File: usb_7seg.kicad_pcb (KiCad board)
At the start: 2 copper layers, 72 x 47.5 mm, 8 parts, among them U1 SeeeduinoXIAO, U2 7segment_led, U3  TM1637 TM1637

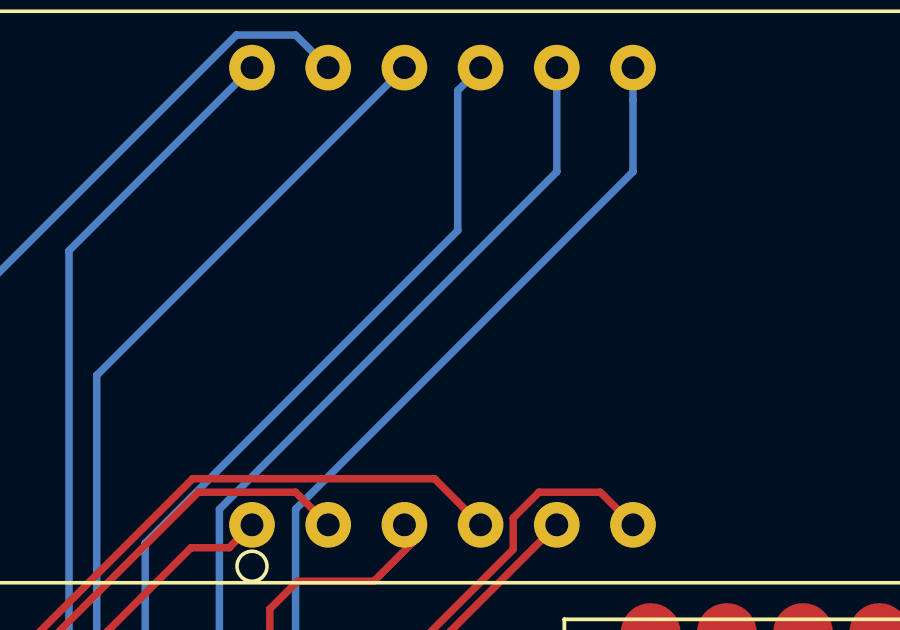
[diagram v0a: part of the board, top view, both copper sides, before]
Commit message: 7セグLEDの極性をシルクで記載した
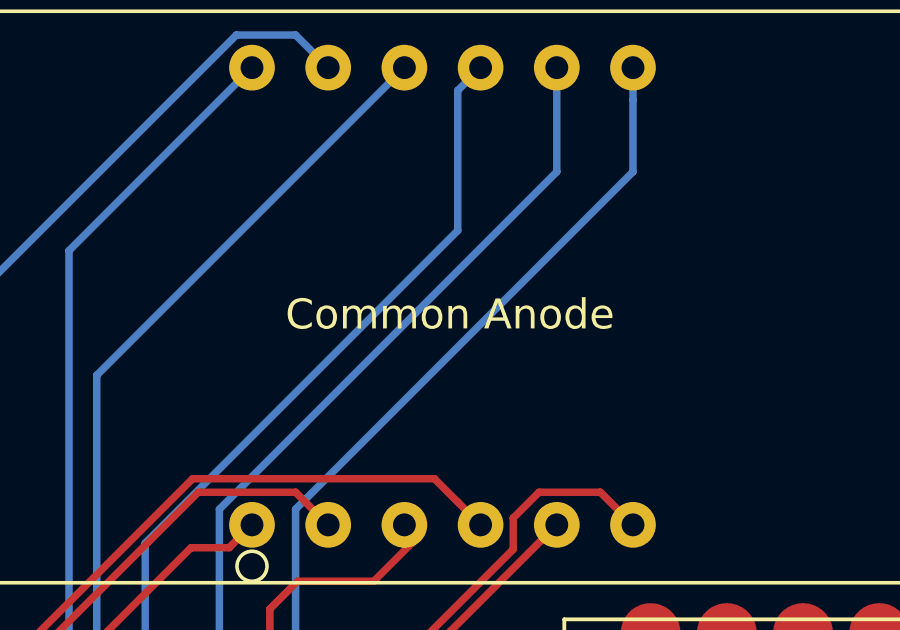
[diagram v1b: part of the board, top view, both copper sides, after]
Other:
- board text added: "Common Anode"
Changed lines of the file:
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@@
   (general
     (thickness 1.6)
-    (drawings 1)
+    (drawings 2)
     (tracks 118)
     (zones 0)
@@
       (net 36 "Net-(U3-Pad10)"))
   )
+  (gr_text "Common Anode" (at 36.83 -34.29) (layer F.SilkS)
+    (effects (font (size 1 1) (thickness 0.15)))
+  )
   (gr_text "2020 REALGLOBE Inc rev 0.3" (at 36.83 -45.72) (layer F.SilkS)
